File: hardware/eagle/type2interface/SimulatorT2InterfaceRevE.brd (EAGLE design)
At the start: 80 x 80 mm, 25 parts, among them IC1 7805T, IC2 MAX233, IC3 ATMEGA328P_PDIP

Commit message: Interface RevE Boards
Eagle files and Gerbers for Type 2 Interface Board Rev E
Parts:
- added Q1: CSTLS8M00G53-B0, murata-resonators:CSTLS_G8
- moved C6 16.5 mm to (35.6, 44.5), turned to 270 degrees
- moved R1 8.98 mm to (26.7, 44.5), turned to 0 degrees
- moved C3 1.27 mm to (35.6, 36.8), turned to 90 degrees
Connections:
- new net OSC1: IC3.9, Q1.1
- new net OSC2: IC3.10, Q1.3
- net GND: now also Q1.2
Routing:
- net RESET: track 61.4 -> 75.4 mm
- net VCC: track 262.4 -> 273.1 mm
- net OSC2: track 0.00 -> 4.32 mm
- net OSC1: track 0.00 -> 4.32 mm
- net TX2: track 24.8 -> 28.5 mm
- net TXD: track 22.2 -> 24.7 mm
- net TX: track 18.0 -> 20.2 mm
- net RX: track 17.8 -> 19.7 mm
- net CRO: track 28.8 -> 30.3 mm
- net RXD: track 27.6 -> 28.5 mm
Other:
- board text added: "Rev E 05/2019"
- board text removed: "Rev D 01/2019"

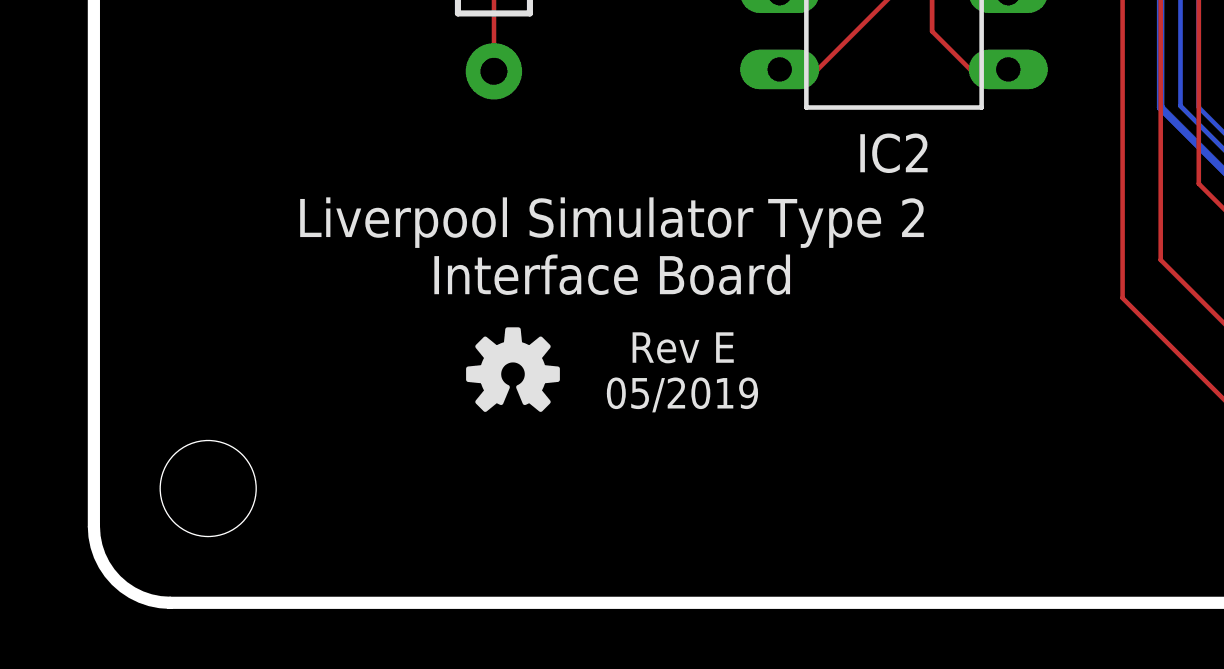
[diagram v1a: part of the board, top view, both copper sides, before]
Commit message: Board Housekeeping
URL on silkscreens, caution messages, tidy up naming conventions.
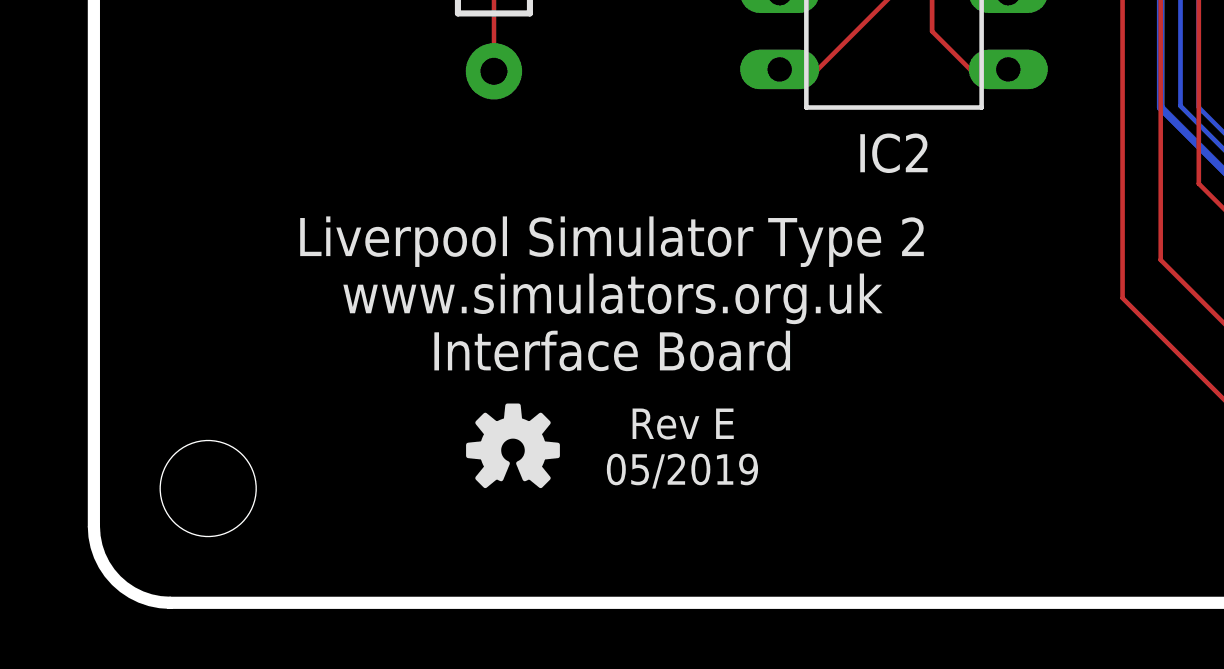
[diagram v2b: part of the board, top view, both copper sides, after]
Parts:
- added U$1: (no value), AIC_Custom:WARNING_TRIANGLE_TPLACE
- moved LOGO1 2.54 mm to (14.0, 5.08)
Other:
- board text added: "Connect this board to Liverpool Simulator Type 2 or compatible equipment ONLY. Refer to documentation for details."
- board text added: "Liverpool Simulator Type 2 www.simulators.org.uk Interface Board"
- board text removed: "Liverpool Simulator Type 2 Interface Board"
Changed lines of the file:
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@@
 <board>
 <plain>
-<text x="17.272" y="10.287" size="1.27" layer="21" font="vector" align="bottom-center">Liverpool Simulator Type 2
+<text x="17.272" y="7.747" size="1.27" layer="21" font="vector" align="bottom-center">Liverpool Simulator Type 2
+www.simulators.org.uk
 Interface Board</text>
-<text x="19.6215" y="6.477" size="1.016" layer="21" font="vector" align="bottom-center">Rev E
+<text x="19.6215" y="3.937" size="1.016" layer="21" font="vector" align="bottom-center">Rev E
 05/2019</text>
 <rectangle x1="22.225" y1="41.91" x2="22.86" y2="42.545" layer="21"/>
@@
 Lead Forming
 Guide</text>
+<text x="66.04" y="40.64" size="1.27" layer="22" font="vector" rot="MR90" align="center">Connect this board to Liverpool Simulator
+Type 2 or compatible equipment ONLY.
+Refer to documentation for details.</text>
 </plain>
 <attributes>
@@
 <attribute name="VALUE" x="43.18" y="65.5828" size="1.27" layer="27" font="vector" rot="R270" align="bottom-center"/>
 </element>
-<element name="LOGO1" library="SparkFun-Aesthetics" package="OSHW-LOGO-S" value="OSHW-LOGOS" x="13.97" y="7.62"/>
+<element name="LOGO1" library="SparkFun-Aesthetics" package="OSHW-LOGO-S" value="OSHW-LOGOS" x="13.97" y="5.08"/>
 <element name="D2" library="AIC_Custom" package="DO41_TVS_UNI" value="SA5.0A" x="58.42" y="72.39" smashed="yes">
 <attribute name="NAME" x="58.42" y="74.041" size="1.27" layer="25" font="vector" align="bottom-center"/>
@@
 <attribute name="NAME" x="34.004" y="32.702" size="1.27" layer="25" font="vector" rot="R270" align="center-right"/>
 </element>
+<element name="U$1" library="AIC_Custom" package="WARNING_TRIANGLE_TPLACE" value="" x="63.5" y="13.97" rot="MR90"/>
 </elements>
 <signals>
@@
 </signal>
 </signals>
+<errors>
+</errors>
 </board>
 </drawing>
